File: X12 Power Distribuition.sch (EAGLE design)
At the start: 43 parts, among them Q1 SPB80P06P, Y1 ECS-80-S-4X

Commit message: altered board
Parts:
- U$5, U$7: device Brickboard_Connector:BRICKBOARD_TSW_14X2 -> Dist_to_Brickboard_Connector:BRICKBOARD_TSW_14X2
- U$6: device Conversion_Connector:CONVERSION_TSW_12X2 -> Dist_to_Conversion_Connector:CONVERSION_TSW_12X2

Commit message: worked on board
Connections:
- removed net ALERT_A: U$5.31
- removed net ALERT_B: U$7.31
- removed net CLK_A: U$5.30
- removed net CLK_B: U$7.30
- removed net DATA_A: U$5.32
- removed net DATA_B: U$7.32
- new net ALERT: U$4.PB7, U$5.31, U$7.31
- new net CLK: U$4.PA9, U$5.30, U$7.30
- new net DATA: U$4.PA10, U$5.32, U$7.32
- net +48V: now also J3.1
- net +48V_RAW: no longer J3.1
- net 3V3GND: now also SV1.3
- net GND: no longer SV1.3
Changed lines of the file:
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@@
 <pinref part="U$7" gate="G$1" pin="14"/>
+</segment>
+<segment>
+<pinref part="J3" gate="G$1" pin="1"/>
+<wire x1="238.76" y1="134.62" x2="228.6" y2="134.62" width="0.1524" layer="91"/>
+<label x="228.6" y="134.62" size="1.778" layer="95" rot="R180" xref="yes"/>
 </segment>
 </net>
@@
 <label x="228.6" y="154.94" size="1.778" layer="95" rot="R180" xref="yes"/>
 </segment>
-<segment>
-<pinref part="J3" gate="G$1" pin="1"/>
-<wire x1="238.76" y1="134.62" x2="228.6" y2="134.62" width="0.1524" layer="91"/>
-<label x="228.6" y="134.62" size="1.778" layer="95" rot="R180" xref="yes"/>
-</segment>
 </net>
 <net name="GND" class="0">
@@
 <wire x1="264.16" y1="83.82" x2="264.16" y2="96.52" width="0.1524" layer="91"/>
 <label x="264.16" y="83.82" size="1.778" layer="95" rot="R180" xref="yes"/>
-</segment>
-<segment>
-<pinref part="SV1" gate="G$1" pin="3"/>
-<wire x1="472.44" y1="78.74" x2="487.68" y2="78.74" width="0.1524" layer="91"/>
-<label x="487.68" y="78.74" size="1.778" layer="95" xref="yes"/>
 </segment>
 <segment>
@@
 </segment>
 </net>
-<net name="CLK_A" class="0">
-<segment>
-<wire x1="134.62" y1="43.18" x2="132.08" y2="43.18" width="0.1524" layer="91"/>
-<label x="134.62" y="43.18" size="1.778" layer="95" xref="yes"/>
-<pinref part="U$5" gate="G$1" pin="30"/>
-</segment>
-</net>
-<net name="DATA_A" class="0">
-<segment>
-<wire x1="137.16" y1="40.64" x2="132.08" y2="40.64" width="0.1524" layer="91"/>
-<label x="144.78" y="40.64" size="1.778" layer="95" xref="yes"/>
-<wire x1="137.16" y1="40.64" x2="144.78" y2="40.64" width="0.1524" layer="91"/>
-<pinref part="U$5" gate="G$1" pin="32"/>
-</segment>
-</net>
 <net name="N$57" class="0">
 <segment>
 <wire x1="104.14" y1="43.18" x2="99.06" y2="43.18" width="0.1524" layer="91"/>
 <pinref part="U$5" gate="G$1" pin="29"/>
-</segment>
-</net>
-<net name="ALERT_A" class="0">
-<segment>
-<wire x1="104.14" y1="40.64" x2="99.06" y2="40.64" width="0.1524" layer="91"/>
-<label x="99.06" y="40.64" size="1.778" layer="95" rot="R180" xref="yes"/>
-<pinref part="U$5" gate="G$1" pin="31"/>
 </segment>
 </net>
@@
 <label x="541.02" y="45.72" size="1.778" layer="95" rot="R270" xref="yes"/>
 </segment>
+<segment>
+<pinref part="SV1" gate="G$1" pin="3"/>
+<wire x1="472.44" y1="78.74" x2="487.68" y2="78.74" width="0.1524" layer="91"/>
+<label x="487.68" y="78.74" size="1.778" layer="95" xref="yes"/>
+</segment>
 </net>
 <net name="N$82" class="0">
@@
 </segment>
 </net>
-<net name="DATA_B" class="0">
+<net name="DATA" class="0">
 <segment>
 <wire x1="137.16" y1="88.9" x2="132.08" y2="88.9" width="0.1524" layer="91"/>
@@
 <pinref part="U$7" gate="G$1" pin="32"/>
 </segment>
-</net>
-<net name="CLK_B" class="0">
+<segment>
+<wire x1="137.16" y1="40.64" x2="132.08" y2="40.64" width="0.1524" layer="91"/>
+<label x="144.78" y="40.64" size="1.778" layer="95" xref="yes"/>
+<wire x1="137.16" y1="40.64" x2="144.78" y2="40.64" width="0.1524" layer="91"/>
+<pinref part="U$5" gate="G$1" pin="32"/>
+</segment>
+<segment>
+<pinref part="U$4" gate="G$1" pin="PA10"/>
+<wire x1="513.08" y1="129.54" x2="523.24" y2="129.54" width="0.1524" layer="91"/>
+<label x="523.24" y="129.54" size="1.778" layer="95" xref="yes"/>
+</segment>
+</net>
+<net name="CLK" class="0">
 <segment>
 <wire x1="134.62" y1="91.44" x2="132.08" y2="91.44" width="0.1524" layer="91"/>
@@
 <pinref part="U$7" gate="G$1" pin="30"/>
 </segment>
-</net>
-<net name="ALERT_B" class="0">
+<segment>
+<wire x1="134.62" y1="43.18" x2="132.08" y2="43.18" width="0.1524" layer="91"/>
+<label x="134.62" y="43.18" size="1.778" layer="95" xref="yes"/>
+<pinref part="U$5" gate="G$1" pin="30"/>
+</segment>
+<segment>
+<pinref part="U$4" gate="G$1" pin="PA9"/>
+<wire x1="513.08" y1="127" x2="533.4" y2="127" width="0.1524" layer="91"/>
+<label x="533.4" y="127" size="1.778" layer="95" xref="yes"/>
+</segment>
+</net>
+<net name="ALERT" class="0">
 <segment>
 <wire x1="104.14" y1="88.9" x2="99.06" y2="88.9" width="0.1524" layer="91"/>
@@
 <pinref part="U$7" gate="G$1" pin="31"/>
 </segment>
-</net>
+<segment>
+<wire x1="104.14" y1="40.64" x2="99.06" y2="40.64" width="0.1524" layer="91"/>
+<label x="99.06" y="40.64" size="1.778" layer="95" rot="R180" xref="yes"/>
+<pinref part="U$5" gate="G$1" pin="31"/>
+</segment>
+<segment>
+<pinref part="U$4" gate="G$1" pin="PB7"/>
+<wire x1="485.14" y1="154.94" x2="485.14" y2="167.64" width="0.1524" layer="91"/>
+<wire x1="485.14" y1="167.64" x2="469.9" y2="167.64" width="0.1524" layer="91"/>
+<label x="469.9" y="167.64" size="1.778" layer="95" rot="R180" xref="yes"/>
+</segment>
+</net>

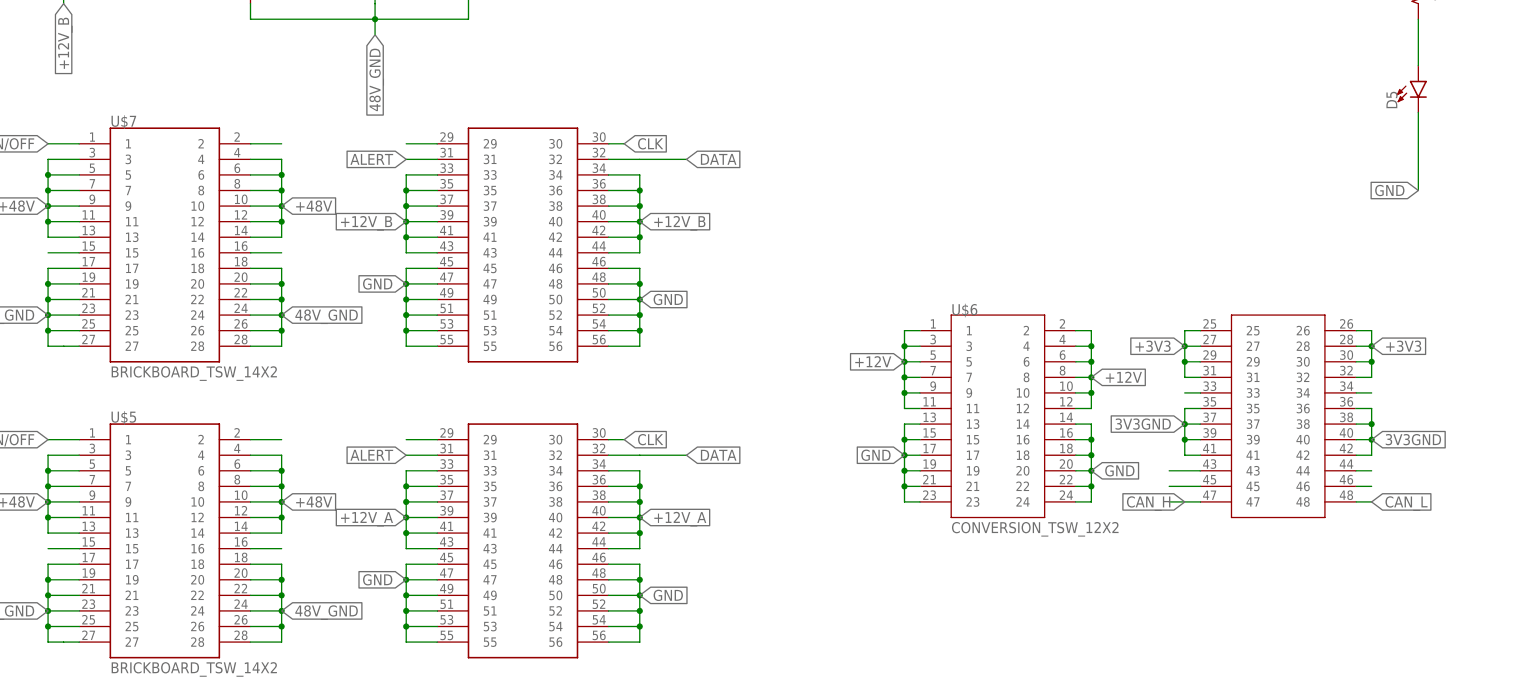
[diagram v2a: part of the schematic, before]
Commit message: updated connector
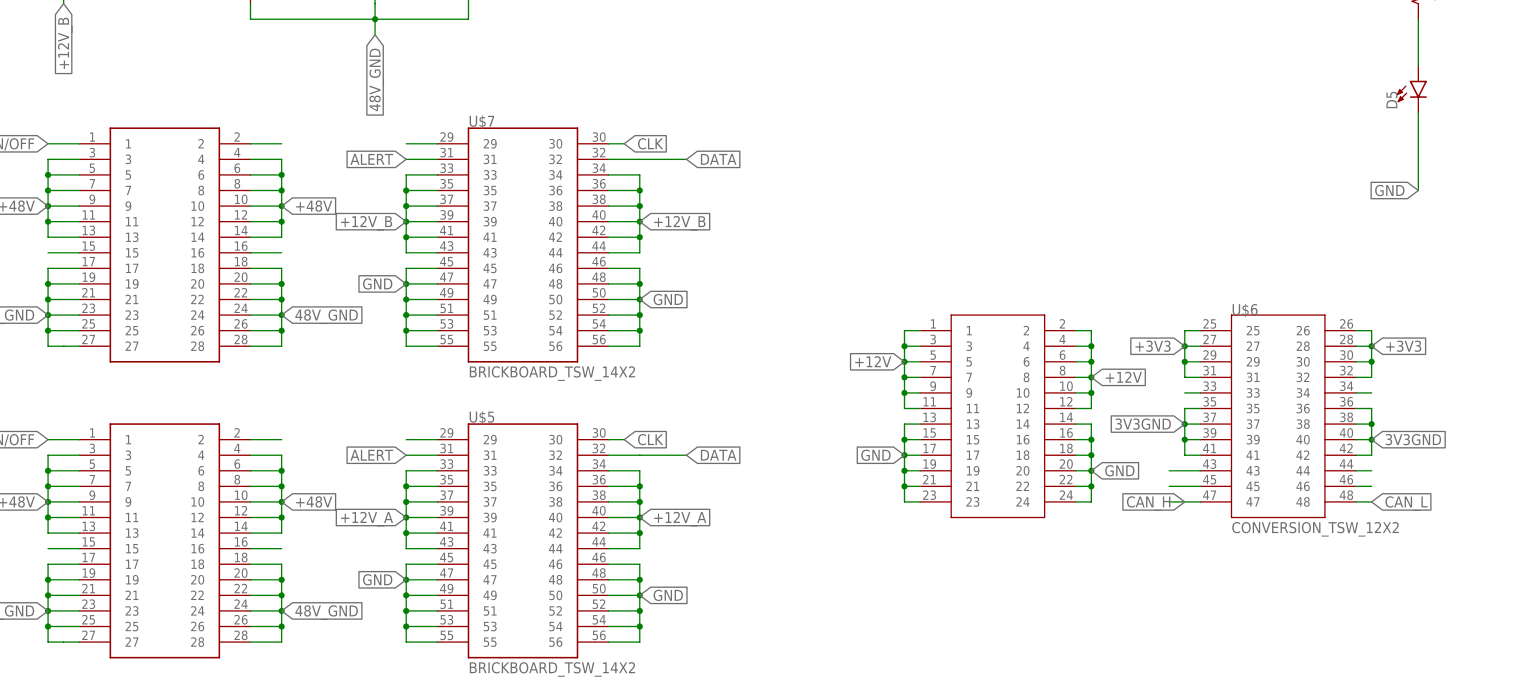
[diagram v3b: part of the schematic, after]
